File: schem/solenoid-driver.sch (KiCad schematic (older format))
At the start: 21 parts, among them P1 CONN_3X2, P3 CONN_2, P4 Chassis GND, U1 MIC2009A-1, U2 ULN2003, U3 MIC2250-2

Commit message: Tune up schema
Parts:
- removed P1: CONN_3X2, ~, symbol solenoid-driver-rescue:CONN_3X2
- removed P3: CONN_2, ~, symbol solenoid-driver-rescue:CONN_2
- removed P4: Chassis GND, ~, symbol solenoid-driver-rescue:CONN_1
- added J?: Conn_01x03, symbol Connector_Generic:Conn_01x03
- added J?: SOLENOID, Connector_PinHeader_2.54mm:PinHeader_1x02_P2.54mm_Vertical, symbol Connector_Generic:Conn_01x02
- C1, C2, C4: footprint ~ -> Capacitor_SMD:C_0805_2012Metric
- C3, C5: footprint ~ -> Capacitor_SMD:C_1206_3216Metric
- C6: footprint ~ -> Capacitor_SMD:CP_Elec_6.3x7.7
- D1: footprint ~ -> Diode_SMD:D_SMA
- L1: footprint ~ -> Inductor_SMD:L_12x12mm_H6mm
- R1, R2, R3, R4, R5, R6: footprint ~ -> Resistor_SMD:R_0805_2012Metric
- U1: footprint ~ -> Package_TO_SOT_SMD:SOT-23-6
- U2: footprint (none) -> Package_SO:SOIC-16_3.9x9.9mm_P1.27mm
- U3: footprint (none) -> Package_TO_SOT_SMD:SOT-23-5
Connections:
- net +5V: now also R6.2, J?.3 (Pin_3)
- net +9V: now also J?.1 (Pin_1)
- net GND: now also J?.1 (Pin_1); no longer R6.2
- net SIGNAL: now reaches U2.1 (I1), U2.2 (I2), U2.3 (I3), U2.4 (I4), U2.5 (I5), U2.6 (I6), U2.7 (I7)
- net at U2.10 (O7), U2.11 (O6), U2.12 (O5)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: now also J?.2 (Pin_2)
- new net SIGNAL': J?.2 (Pin_2)
- no-connect marks 2 -> 0
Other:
- note added: "Always pull up ENABLE, since\nsolenoid toggle is done via\nQMK firmware"
- moved on the sheet: R6
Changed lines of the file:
@@
 $EndDescr
-$Comp
-L solenoid-driver-rescue:CONN_3X2 P1
-U 1 1 533CF06C
-P 2350 4350
-F 0 "P1" H 2350 4600 50  0000 C CNN
-F 1 "CONN_3X2" V 2350 4400 40  0000 C CNN
-F 2 "~" H 2350 4350 60  0000 C CNN
-F 3 "~" H 2350 4350 60  0000 C CNN
-	1    2350 4350
-	1    0    0    -1
-$EndComp
-$Comp
-L solenoid-driver-rescue:GND #PWR01
-U 1 1 533CF0AA
-P 2800 4450
-F 0 "#PWR01" H 2800 4450 30  0001 C CNN
-F 1 "GND" H 2800 4380 30  0001 C CNN
-F 2 "" H 2800 4450 60  0000 C CNN
-F 3 "" H 2800 4450 60  0000 C CNN
-	1    2800 4450
-	1    0    0    -1
-$EndComp
-$Comp
-L power:+5V #PWR02
-U 1 1 533CF0E2
-P 1900 4150
-F 0 "#PWR02" H 1900 4240 20  0001 C CNN
-F 1 "+5V" H 1900 4240 30  0000 C CNN
-F 2 "" H 1900 4150 60  0000 C CNN
-F 3 "" H 1900 4150 60  0000 C CNN
-	1    1900 4150
-	1    0    0    -1
-$EndComp
-NoConn ~ 1950 4300
-NoConn ~ 1950 4400
 $Comp
 L solenoid-driver-rescue:ULN2003 U2
@@
 F 0 "U2" H 5650 4800 70  0000 C CNN
 F 1 "ULN2003" H 5650 4400 70  0000 C CNN
-F 2 "" H 5650 4700 60  0000 C CNN
+F 2 "Package_SO:SOIC-16_3.9x9.9mm_P1.27mm" H 5650 4700 60  0000 C CNN
 F 3 "" H 5650 4700 60  0000 C CNN
 	1    5650 4700
-	1    0    0    -1
-$EndComp
-$Comp
-L solenoid-driver-rescue:CONN_2 P3
-U 1 1 533CF848
-P 7050 4800
-F 0 "P3" V 7000 4800 40  0000 C CNN
-F 1 "CONN_2" V 7100 4800 40  0000 C CNN
-F 2 "~" H 7050 4800 60  0000 C CNN
-F 3 "~" H 7050 4800 60  0000 C CNN
-	1    7050 4800
 	1    0    0    -1
 $EndComp
@@
 F 0 "R3" V 7130 4300 40  0000 C CNN
 F 1 "470" V 7057 4301 40  0000 C CNN
-F 2 "~" V 6980 4300 30  0000 C CNN
+F 2 "Resistor_SMD:R_0805_2012Metric" V 6980 4300 30  0000 C CNN
 F 3 "~" H 7050 4300 30  0000 C CNN
 	1    7050 4300
@@
 F 0 "C2" H 2450 2800 40  0000 L CNN
 F 1 "0.1uF" H 2456 2615 40  0000 L CNN
-F 2 "~" H 2488 2550 30  0000 C CNN
+F 2 "Capacitor_SMD:C_0805_2012Metric" H 2488 2550 30  0000 C CNN
 F 3 "~" H 2450 2700 60  0000 C CNN
 	1    2450 2700
@@
 F 0 "C4" H 6350 5450 40  0000 L CNN
 F 1 "0.1uF" H 6356 5265 40  0000 L CNN
-F 2 "~" H 6388 5200 30  0000 C CNN
+F 2 "Capacitor_SMD:C_0805_2012Metric" H 6388 5200 30  0000 C CNN
 F 3 "~" H 6350 5350 60  0000 C CNN
 	1    6350 5350
@@
 F 0 "U1" H 3700 2900 60  0000 L CNN
 F 1 "MIC2009A-1" H 3950 2400 60  0000 C CNN
-F 2 "~" H 3900 2650 60  0000 C CNN
+F 2 "Package_TO_SOT_SMD:SOT-23-6" H 3900 2650 60  0000 C CNN
 F 3 "~" H 3900 2650 60  0000 C CNN
 	1    3950 2650
@@
 F 0 "R1" V 4730 3100 40  0000 C CNN
 F 1 "470" V 4657 3101 40  0000 C CNN
-F 2 "~" V 4580 3100 30  0000 C CNN
+F 2 "Resistor_SMD:R_0805_2012Metric" V 4580 3100 30  0000 C CNN
 F 3 "~" H 4650 3100 30  0000 C CNN
 	1    4650 3100
@@
 F 0 "R2" V 5530 3050 40  0000 C CNN
 F 1 "100K" V 5457 3051 40  0000 C CNN
-F 2 "~" V 5380 3050 30  0000 C CNN
+F 2 "Resistor_SMD:R_0805_2012Metric" V 5380 3050 30  0000 C CNN
 F 3 "~" H 5450 3050 30  0000 C CNN
 	1    5450 3050
@@
 F 0 "U3" H 7100 2900 60  0000 L CNN
 F 1 "MIC2250-2" H 6950 2400 60  0000 C CNN
-F 2 "" H 6900 2650 60  0000 C CNN
+F 2 "Package_TO_SOT_SMD:SOT-23-5" H 6900 2650 60  0001 C CNN
 F 3 "" H 6900 2650 60  0000 C CNN
 	1    6950 2650
@@
 F 0 "C1" H 2150 2800 40  0000 L CNN
 F 1 "1uF" H 2156 2615 40  0000 L CNN
-F 2 "~" H 2188 2550 30  0000 C CNN
+F 2 "Capacitor_SMD:C_0805_2012Metric" H 2188 2550 30  0000 C CNN
 F 3 "~" H 2150 2700 60  0000 C CNN
 	1    2150 2700
@@
 F 0 "C3" H 6100 2950 40  0000 L CNN
 F 1 "22uF" H 6106 2765 40  0000 L CNN
-F 2 "~" H 6138 2700 30  0000 C CNN
+F 2 "Capacitor_SMD:C_1206_3216Metric" H 6138 2700 30  0000 C CNN
 F 3 "~" H 6100 2850 60  0000 C CNN
 	1    6100 2850
@@
 F 0 "L1" H 6950 2300 50  0000 C CNN
 F 1 "22uH" H 6950 2150 50  0000 C CNN
-F 2 "~" H 6950 2200 60  0000 C CNN
+F 2 "Inductor_SMD:L_12x12mm_H6mm" H 6950 2200 60  0000 C CNN
 F 3 "~" H 6950 2200 60  0000 C CNN
 	1    6950 2200
@@
 F 0 "D1" H 7850 2650 40  0000 C CNN
 F 1 "B220A" H 7850 2450 40  0000 C CNN
-F 2 "~" H 7850 2550 60  0000 C CNN
+F 2 "Diode_SMD:D_SMA" H 7850 2550 60  0000 C CNN
 F 3 "~" H 7850 2550 60  0000 C CNN
 	1    7850 2550
@@
 F 0 "R4" V 8180 2850 40  0000 C CNN
 F 1 "100K" V 8107 2851 40  0000 C CNN
-F 2 "~" V 8030 2850 30  0000 C CNN
+F 2 "Resistor_SMD:R_0805_2012Metric" V 8030 2850 30  0000 C CNN
 F 3 "~" H 8100 2850 30  0000 C CNN
 	1    8100 2850
@@
 F 0 "R5" V 8180 3450 40  0000 C CNN
 F 1 "16K" V 8107 3451 40  0000 C CNN
-F 2 "~" V 8030 3450 30  0000 C CNN
+F 2 "Resistor_SMD:R_0805_2012Metric" V 8030 3450 30  0000 C CNN
 F 3 "~" H 8100 3450 30  0000 C CNN
 	1    8100 3450
@@
 F 0 "C5" H 8350 2900 40  0000 L CNN
 F 1 "22uF" H 8356 2715 40  0000 L CNN
-F 2 "~" H 8388 2650 30  0000 C CNN
+F 2 "Capacitor_SMD:C_1206_3216Metric" H 8388 2650 30  0000 C CNN
 F 3 "~" H 8350 2800 60  0000 C CNN
 	1    8350 2800
@@
 F 0 "C6" H 8700 2900 40  0000 L CNN
 F 1 "220uF" H 8700 2700 40  0000 L CNN
-F 2 "~" H 8750 2650 30  0000 C CNN
+F 2 "Capacitor_SMD:CP_Elec_6.3x7.7" H 8750 2650 30  0000 C CNN
 F 3 "~" H 8650 2800 300 0000 C CNN
 	1    8650 2800
@@
 MIC2250-2 version has frequency\ndithering to reduce EMI.
 $Comp
-L power:PWR_FLAG #FLG014
-U 1 1 533FB7F8
-P 1650 4150
-F 0 "#FLG014" H 1650 4245 30  0001 C CNN
-F 1 "PWR_FLAG" H 1650 4330 30  0000 C CNN
-F 2 "" H 1650 4150 60  0000 C CNN
-F 3 "" H 1650 4150 60  0000 C CNN
-	1    1650 4150
-	1    0    0    -1
-$EndComp
-$Comp
-L power:PWR_FLAG #FLG015
-U 1 1 533FBA37
-P 2950 4450
-F 0 "#FLG015" H 2950 4545 30  0001 C CNN
-F 1 "PWR_FLAG" H 2950 4630 30  0000 C CNN
-F 2 "" H 2950 4450 60  0000 C CNN
-F 3 "" H 2950 4450 60  0000 C CNN
-	1    2950 4450
-	-1   0    0    1
-$EndComp
-$Comp
 L power:PWR_FLAG #FLG016
 U 1 1 533FBB83
@@
 $EndComp
 Wire Wire Line
-	1900 4150 1900 4200
-Wire Wire Line
-	1650 4200 1900 4200
-Wire Wire Line
-	2750 4400 2800 4400
-Wire Wire Line
-	2800 4400 2800 4450
-Wire Wire Line
 	4950 4300 4950 4400
 Wire Wire Line
@@
 Wire Wire Line
 	6350 4800 6300 4800
-Connection ~ 4950 4300
 Wire Wire Line
 	6350 5050 6350 5100
@@
 Connection ~ 6100 2550
 Wire Wire Line
-	1650 4200 1650 4150
-Connection ~ 1900 4200
-Wire Wire Line
-	2950 4400 2950 4450
-Connection ~ 2800 4400
-Wire Wire Line
 	9150 2550 9150 2500
 Connection ~ 8950 2550
 Wire Wire Line
 	3200 2450 3200 2550
-Wire Wire Line
-	2750 4300 4950 4300
-Wire Wire Line
-	3000 2750 3300 2750
-Wire Wire Line
-	3300 2750 3300 4200
-Wire Wire Line
-	3300 4200 2750 4200
 Wire Wire Line
 	6350 4400 6350 4500
@@
 SW
 $Comp
-L solenoid-driver-rescue:CONN_1 P4
-U 1 1 5340C7FE
-P 3150 4400
-F 0 "P4" H 3230 4400 40  0000 L CNN
-F 1 "Chassis GND" H 3150 4455 30  0000 C CNN
-F 2 "~" H 3150 4400 60  0000 C CNN
-F 3 "~" H 3150 4400 60  0000 C CNN
-	1    3150 4400
-	1    0    0    -1
-$EndComp
-Connection ~ 2950 4400
-$Comp
 L solenoid-driver-rescue:R R6
 U 1 1 536DB50B
-P 3000 3050
-F 0 "R6" V 3080 3050 40  0000 C CNN
-F 1 "100K" V 3007 3051 40  0000 C CNN
-F 2 "~" V 2930 3050 30  0000 C CNN
-F 3 "~" H 3000 3050 30  0000 C CNN
-	1    3000 3050
-	1    0    0    -1
-$EndComp
-Wire Wire Line
-	3000 2800 3000 2750
-Connection ~ 3300 2750
-$Comp
-L solenoid-driver-rescue:GND #PWR021
-U 1 1 536DB5BC
-P 3000 3300
-F 0 "#PWR021" H 3000 3300 30  0001 C CNN
-F 1 "GND" H 3000 3230 30  0001 C CNN
-F 2 "" H 3000 3300 60  0000 C CNN
-F 3 "" H 3000 3300 60  0000 C CNN
-	1    3000 3300
+P 3200 3000
+F 0 "R6" V 3280 3000 40  0000 C CNN
+F 1 "100K" V 3207 3001 40  0000 C CNN
+F 2 "Resistor_SMD:R_0805_2012Metric" V 3130 3000 30  0000 C CNN
+F 3 "~" H 3200 3000 30  0000 C CNN
+	1    3200 3000
 	1    0    0    -1
 $EndComp
@@
 	6350 5100 6350 5150
 Wire Wire Line
-	2450 2450 3200 2450
+	2450 2450 2825 2450
 Wire Wire Line
 	2300 2450 2450 2450
@@
 	6100 2550 6300 2550
 Wire Wire Line
-	1900 4200 1950 4200
-Wire Wire Line
-	2800 4400 2950 4400
-Wire Wire Line
 	8950 2550 9150 2550
 Wire Wire Line
@@
 	6350 4900 6700 4900
 Wire Wire Line
-	2950 4400 3000 4400
-Wire Wire Line
-	3300 2750 3350 2750
-Wire Wire Line
 	5450 3350 6300 3350
+Wire Wire Line
+	2825 2450 2825 3250
+Connection ~ 2825 2450
+Wire Wire Line
+	2825 2450 3200 2450
+Text Notes 1950 3600 0    50   ~ 0
+Always pull up ENABLE, since\nsolenoid toggle is done via\nQMK firmware
+Wire Wire Line
+	3200 2750 3350 2750
+Wire Wire Line
+	2825 3250 3200 3250
+$Comp
+L Connector_Generic:Conn_01x03 J?
+U 1 1 5E7C9766
+P 3275 4600
+F 0 "J?" H 3193 4275 50  0000 C CNN
+F 1 "Conn_01x03" H 3193 4366 50  0000 C CNN
+F 2 "" H 3275 4600 50  0001 C CNN
+F 3 "~" H 3275 4600 50  0001 C CNN
+	1    3275 4600
+	-1   0    0    1
+$EndComp
+Text GLabel 3475 4600 2    50   Input ~ 0
+SIGNAL'
+$Comp
+L power:+5V #PWR?
+U 1 1 5E7CB7F0
+P 3650 4500
+F 0 "#PWR?" H 3650 4350 50  0001 C CNN
+F 1 "+5V" H 3665 4673 50  0000 C CNN
+F 2 "" H 3650 4500 50  0001 C CNN
+F 3 "" H 3650 4500 50  0001 C CNN
+	1    3650 4500
+	1    0    0    -1
+$EndComp
+Wire Wire Line
+	3650 4500 3475 4500
+$Comp
+L power:GND #PWR?
+U 1 1 5E7CDEDA
+P 3650 4700
+F 0 "#PWR?" H 3650 4450 50  0001 C CNN
+F 1 "GND" H 3655 4527 50  0000 C CNN
+F 2 "" H 3650 4700 50  0001 C CNN
+F 3 "" H 3650 4700 50  0001 C CNN
+	1    3650 4700
+	1    0    0    -1
+$EndComp
+Wire Wire Line
+	3650 4700 3475 4700
+Text GLabel 4400 4300 0    50   Input ~ 0
+SIGNAL
+Wire Wire Line
+	4400 4300 4950 4300
+Connection ~ 4950 4300
+$Comp
+L Connector_Generic:Conn_01x02 J?
+U 1 1 5E7D9A18
+P 6900 4800
+F 0 "J?" H 6980 4792 50  0000 L CNN
+F 1 "SOLENOID" H 6980 4701 50  0000 L CNN
+F 2 "Connector_PinHeader_2.54mm:PinHeader_1x02_P2.54mm_Vertical" H 6900 4800 50  0001 C CNN
+F 3 "~" H 6900 4800 50  0001 C CNN
+	1    6900 4800
+	1    0    0    -1
+$EndComp
+Wire Wire Line
+	6700 4700 6700 4800
 $EndSCHEMATC

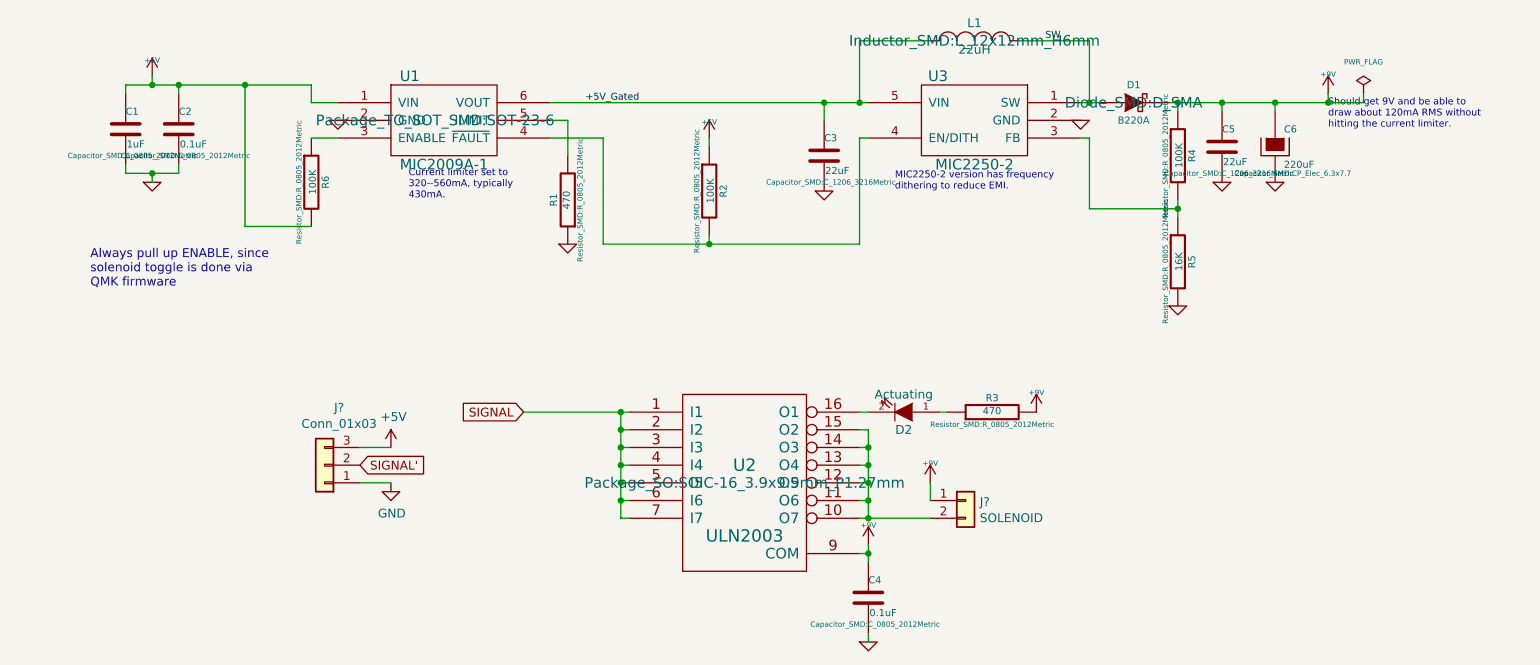
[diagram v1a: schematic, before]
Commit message: Route the PCB
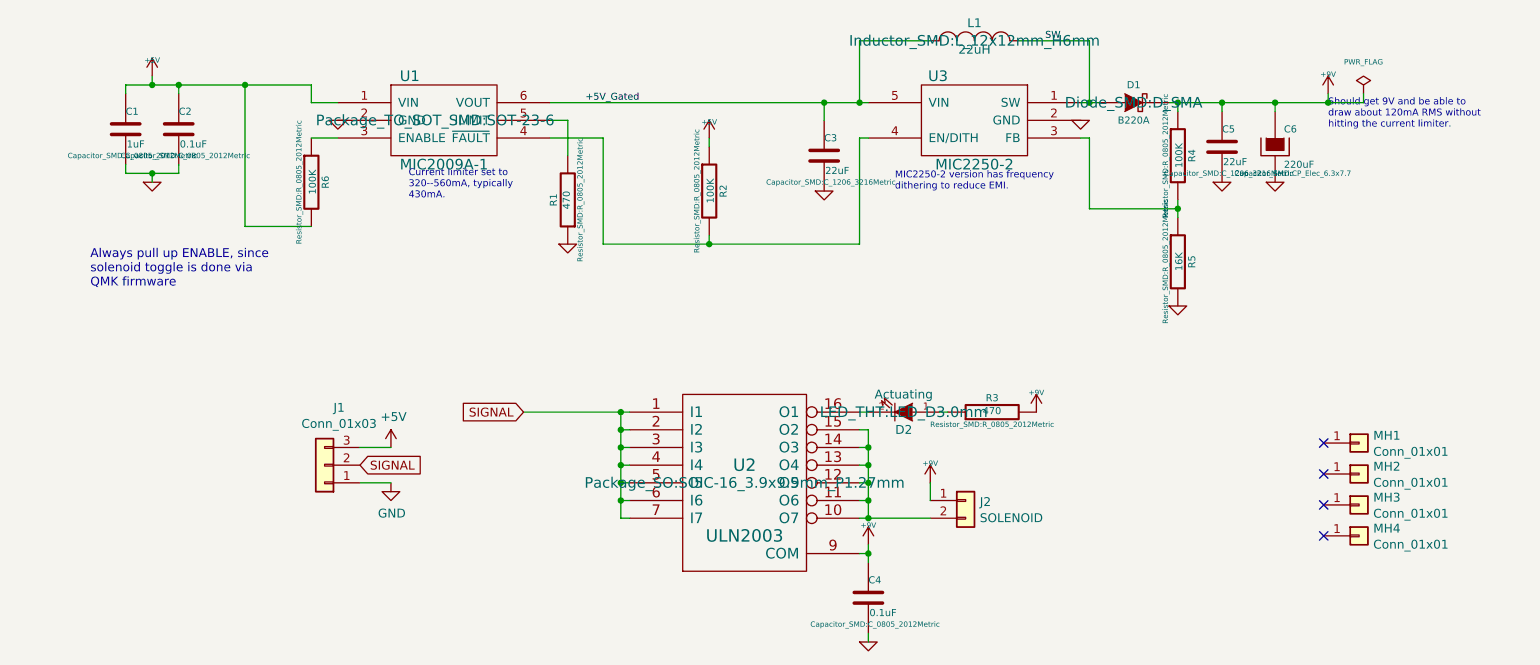
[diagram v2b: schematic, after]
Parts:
- added MH1, MH2, MH3, MH4: Conn_01x01, random-keyboard-parts:Generic-Mounthole, symbol Connector_Generic:Conn_01x01
- D2: footprint ~ -> LED_THT:LED_D3.0mm
- J1: renamed from J?; footprint (none) -> random-keyboard-parts:JST-SR-3
- gave numbers to parts that had none: 1
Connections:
- net SIGNAL' is gone; now on net SIGNAL: J1.2 (Pin_2)
- no-connect marks 0 -> 4
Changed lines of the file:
@@
 $EndDescr
-$Comp
-L solenoid-driver-rescue:ULN2003 U2
-U 1 1 533CF28C
-P 5650 4700
-F 0 "U2" H 5650 4800 70  0000 C CNN
-F 1 "ULN2003" H 5650 4400 70  0000 C CNN
-F 2 "Package_SO:SOIC-16_3.9x9.9mm_P1.27mm" H 5650 4700 60  0000 C CNN
-F 3 "" H 5650 4700 60  0000 C CNN
-	1    5650 4700
-	1    0    0    -1
-$EndComp
 $Comp
 L solenoid-driver-rescue:R R3
@@
 F 0 "D2" H 6550 4400 50  0000 C CNN
 F 1 "Actuating" H 6550 4200 50  0000 C CNN
-F 2 "~" H 6550 4300 60  0000 C CNN
+F 2 "LED_THT:LED_D3.0mm" H 6550 4300 60  0000 C CNN
 F 3 "~" H 6550 4300 60  0000 C CNN
 	1    6550 4300
@@
 	2825 3250 3200 3250
 $Comp
-L Connector_Generic:Conn_01x03 J?
+L Connector_Generic:Conn_01x03 J1
 U 1 1 5E7C9766
 P 3275 4600
-F 0 "J?" H 3193 4275 50  0000 C CNN
+F 0 "J1" H 3193 4275 50  0000 C CNN
 F 1 "Conn_01x03" H 3193 4366 50  0000 C CNN
-F 2 "" H 3275 4600 50  0001 C CNN
+F 2 "random-keyboard-parts:JST-SR-3" H 3275 4600 50  0001 C CNN
 F 3 "~" H 3275 4600 50  0001 C CNN
 	1    3275 4600
@@
 $EndComp
 Text GLabel 3475 4600 2    50   Input ~ 0
-SIGNAL'
-$Comp
-L power:+5V #PWR?
+SIGNAL
+$Comp
+L power:+5V #PWR0101
 U 1 1 5E7CB7F0
 P 3650 4500
-F 0 "#PWR?" H 3650 4350 50  0001 C CNN
+F 0 "#PWR0101" H 3650 4350 50  0001 C CNN
 F 1 "+5V" H 3665 4673 50  0000 C CNN
 F 2 "" H 3650 4500 50  0001 C CNN
@@
 	3650 4500 3475 4500
 $Comp
-L power:GND #PWR?
+L power:GND #PWR0102
 U 1 1 5E7CDEDA
 P 3650 4700
-F 0 "#PWR?" H 3650 4450 50  0001 C CNN
+F 0 "#PWR0102" H 3650 4450 50  0001 C CNN
 F 1 "GND" H 3655 4527 50  0000 C CNN
 F 2 "" H 3650 4700 50  0001 C CNN
@@
 Connection ~ 4950 4300
 $Comp
-L Connector_Generic:Conn_01x02 J?
+L Connector_Generic:Conn_01x02 J2
 U 1 1 5E7D9A18
 P 6900 4800
-F 0 "J?" H 6980 4792 50  0000 L CNN
+F 0 "J2" H 6980 4792 50  0000 L CNN
 F 1 "SOLENOID" H 6980 4701 50  0000 L CNN
 F 2 "Connector_PinHeader_2.54mm:PinHeader_1x02_P2.54mm_Vertical" H 6900 4800 50  0001 C CNN
@@
 Wire Wire Line
 	6700 4700 6700 4800
+$Comp
+L Connector_Generic:Conn_01x01 MH1
+U 1 1 5E804DB7
+P 9125 4475
+F 0 "MH1" H 9205 4517 50  0000 L CNN
+F 1 "Conn_01x01" H 9205 4426 50  0000 L CNN
+F 2 "random-keyboard-parts:Generic-Mounthole" H 9125 4475 50  0001 C CNN
+F 3 "~" H 9125 4475 50  0001 C CNN
+	1    9125 4475
+	1    0    0    -1
+$EndComp
+NoConn ~ 8925 4475
+$Comp
+L Connector_Generic:Conn_01x01 MH2
+U 1 1 5E80A074
+P 9125 4650
+F 0 "MH2" H 9205 4692 50  0000 L CNN
+F 1 "Conn_01x01" H 9205 4601 50  0000 L CNN
+F 2 "random-keyboard-parts:Generic-Mounthole" H 9125 4650 50  0001 C CNN
+F 3 "~" H 9125 4650 50  0001 C CNN
+	1    9125 4650
+	1    0    0    -1
+$EndComp
+NoConn ~ 8925 4650
+$Comp
+L Connector_Generic:Conn_01x01 MH3
+U 1 1 5E80C532
+P 9125 4825
+F 0 "MH3" H 9205 4867 50  0000 L CNN
+F 1 "Conn_01x01" H 9205 4776 50  0000 L CNN
+F 2 "random-keyboard-parts:Generic-Mounthole" H 9125 4825 50  0001 C CNN
+F 3 "~" H 9125 4825 50  0001 C CNN
+	1    9125 4825
+	1    0    0    -1
+$EndComp
+NoConn ~ 8925 4825
+$Comp
+L Connector_Generic:Conn_01x01 MH4
+U 1 1 5E80C539
+P 9125 5000
+F 0 "MH4" H 9205 5042 50  0000 L CNN
+F 1 "Conn_01x01" H 9205 4951 50  0000 L CNN
+F 2 "random-keyboard-parts:Generic-Mounthole" H 9125 5000 50  0001 C CNN
+F 3 "~" H 9125 5000 50  0001 C CNN
+	1    9125 5000
+	1    0    0    -1
+$EndComp
+NoConn ~ 8925 5000
+$Comp
+L solenoid-driver-rescue:ULN2003 U2
+U 1 1 533CF28C
+P 5650 4700
+F 0 "U2" H 5650 4800 70  0000 C CNN
+F 1 "ULN2003" H 5650 4400 70  0000 C CNN
+F 2 "Package_SO:SOIC-16_3.9x9.9mm_P1.27mm" H 5650 4700 60  0000 C CNN
+F 3 "" H 5650 4700 60  0000 C CNN
+	1    5650 4700
+	1    0    0    -1
+$EndComp
 $EndSCHEMATC

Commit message: Finalize PCB
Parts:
- removed C4: 0.1uF, Capacitor_SMD:C_0805_2012Metric, symbol solenoid-driver-rescue:C
- removed D2: Actuating, LED_THT:LED_D3.0mm, symbol solenoid-driver-rescue:LED
- removed R3: 470, Resistor_SMD:R_0805_2012Metric, symbol solenoid-driver-rescue:R
- removed R6: 100K, Resistor_SMD:R_0805_2012Metric, symbol solenoid-driver-rescue:R
- removed U2: ULN2003, Package_SO:SOIC-16_3.9x9.9mm_P1.27mm, symbol solenoid-driver-rescue:ULN2003
- added C7: 10uF, Capacitor_SMD:C_0805_2012Metric, symbol Device:C_Small
- added D?: RB060T, Diode_SMD:D_SOD-123, symbol Device:D_Small
- added Q1: AO3400, Package_TO_SOT_SMD:SOT-23, symbol Device:Q_NMOS_GSD
- added R3: 100K, Resistor_SMD:R_0805_2012Metric, symbol Device:R_Small
- added R6: 270k, Resistor_SMD:R_0805_2012Metric, symbol Device:R_Small
- added R7: 100, Resistor_SMD:R_0805_2012Metric, symbol Device:R_Small
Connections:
- net +5V: now also R6.2
- net +9V: now also D?.1 (K)
- net GND: now also C7.2, Q1.2 (S), R3.1
- net SIGNAL: now also R7.2
- net at J2.2 (Pin_2): now also D?.2 (A), Q1.3 (D)
- net ENABLE: now reaches U1.3 (ENABLE)
- net ENABLE: now also C7.1, R6.1
- new net: Q1.1 (G), R3.2, R7.1
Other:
- note added: "Delayed enable for MIC2009A\nAround 1s before ENABLE exceeds 1.5V"
- note removed: "Always pull up ENABLE, since\nsolenoid toggle is done via\nQMK firmware"
- moved on the sheet: J1, J2, MH1, MH2, MH3, MH4
